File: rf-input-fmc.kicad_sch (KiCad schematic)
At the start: 0 parts

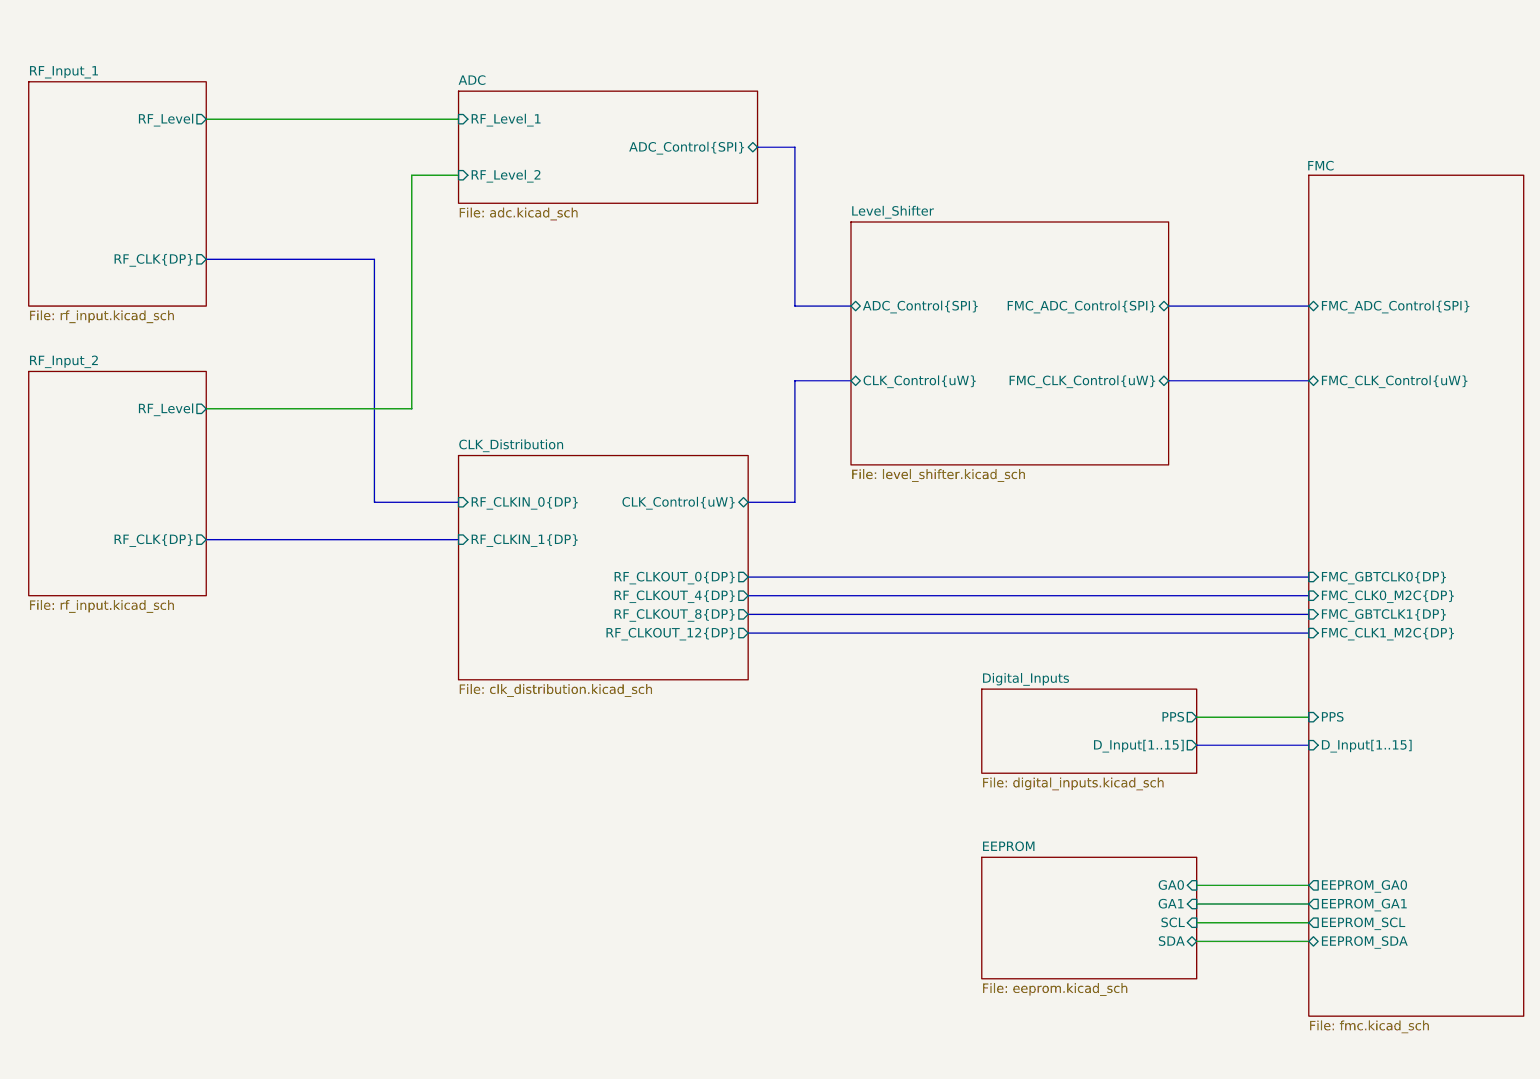
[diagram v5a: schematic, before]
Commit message: Changed ADC and removed Level Shifter
- Changed ADC to ADS7253
- Removed Level Shifters
- Change paper size to US standard sizes for printing
- removed 3d models
- Changed SMA clock input to a 2 pin ISORATE connector
- Floor planned out the PCB layout with the new parts
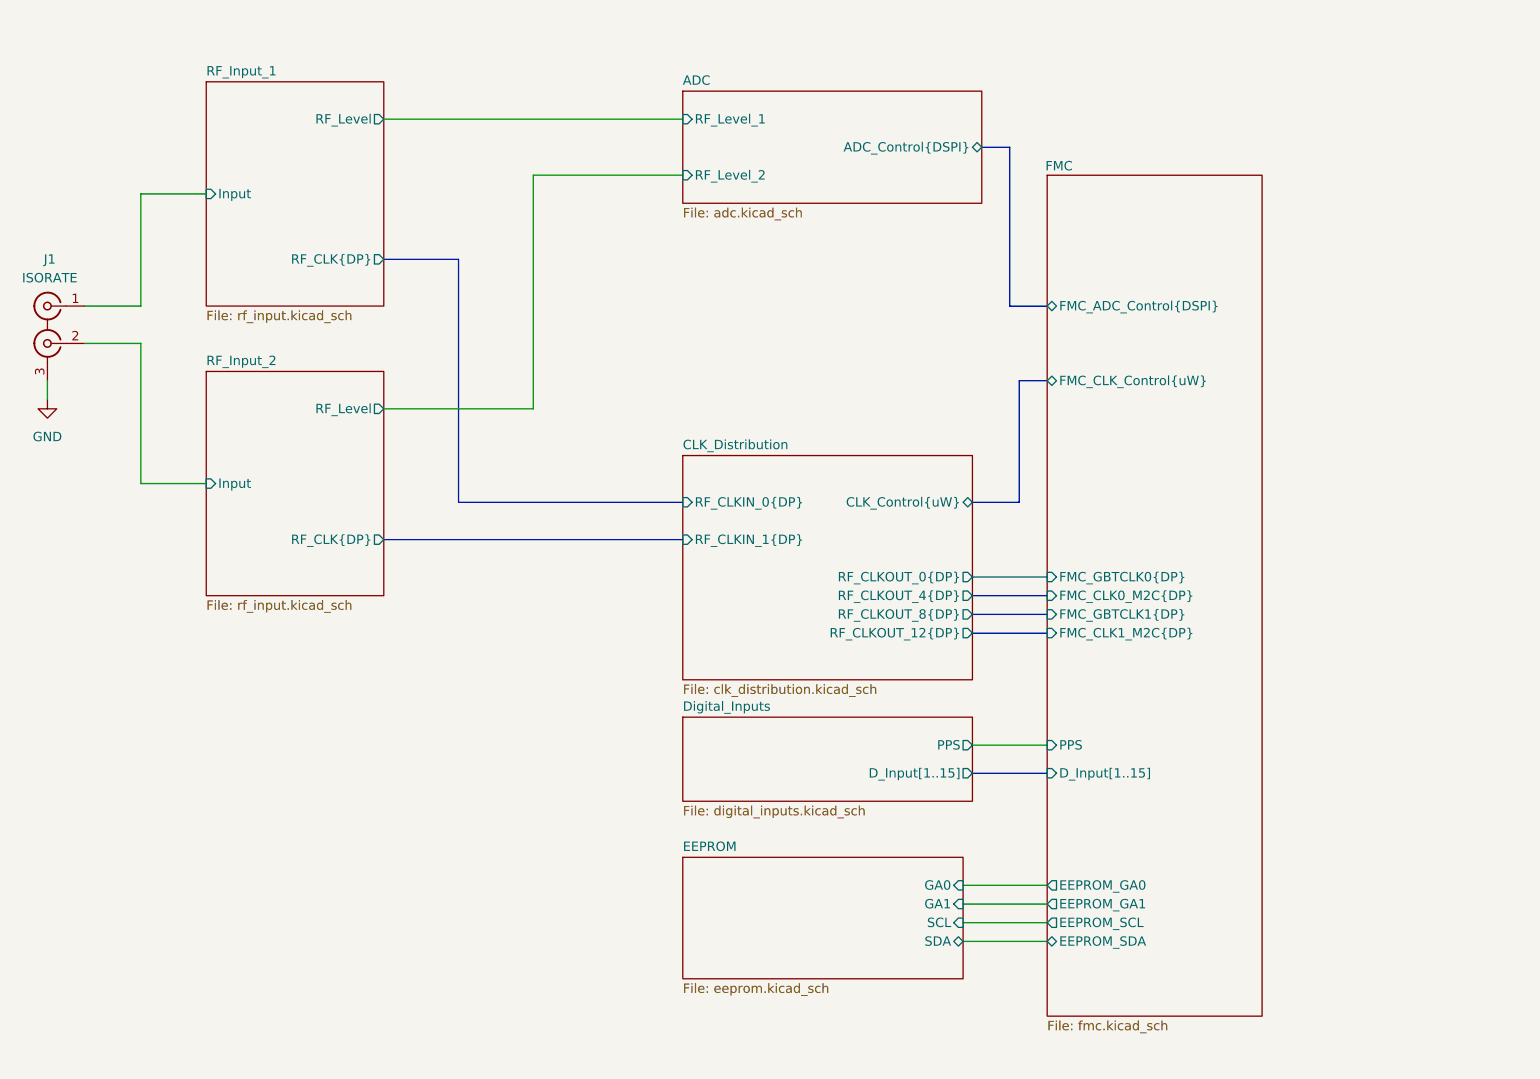
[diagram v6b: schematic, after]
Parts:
- added J1: ISORATE, rf-input-fmc:SAMTEC_IP5-02-01-L-S-RA1-L-TR, symbol Connector:Conn_Coaxial_x2
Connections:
- new net GND: J1.3 (EXT)
- new net RF_Input_1/Input: J1.1 (IN1)
- new net RF_Input_2/Input: J1.2 (IN2)
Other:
- removed sheet Level_Shifter
- sheet ADC ports: added ADC_Control{DSPI}; removed ADC_Control{SPI}
- sheet FMC ports: added FMC_ADC_Control{DSPI}; removed FMC_ADC_Control{SPI}
- sheet RF_Input_1 ports: added Input; removed none
- sheet RF_Input_2 ports: added Input; removed none

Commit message: Final Schmatic Draft
-Changed ADC
-Changed Digital IO Translator
-Updated all MPNs
- Reannoted Schematic
- Updated Design Document
- Added new Datasheet Document
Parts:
- J1: MPN (none) -> SAMTEC_IP5-02-01-L-S-RA1-L-TR; Manufacturer (none) -> Samtec
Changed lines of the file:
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@@
 			)
 		)
-		(property "Datasheet" ""
+		(property "Datasheet" "~"
 			(at 40.64 66.04 0)
 			(effects
@@
 			(at 40.64 63.5 0)
 			(effects
+				(font
+					(size 1.27 1.27)
+				)
+				(hide yes)
+			)
+		)
+		(property "MPN" "SAMTEC_IP5-02-01-L-S-RA1-L-TR"
+			(at 40.64 63.5 0)
+			(effects
+				(font
+					(size 1.27 1.27)
+				)
+				(hide yes)
+			)
+		)
+		(property "Manufacturer" "Samtec"
+			(at 40.64 63.5 0)
+			(effects

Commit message: Schematic updates
- Changed Connecters to MMCX
- Added Test points on clocks and data buses
- Added attenuation before the RF input level detection IC to better keep the recommended input within its linear range
- Added a low pass filter at the input of the RF input level detection IC
- grounded the thermal pad of the ADC
- added some additional decoupling caps in for the clock splitter chip (to be in line with what is on Zest)
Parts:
- removed J1: ISORATE, rf-input-fmc:SAMTEC_IP5-02-01-L-S-RA1-L-TR, symbol Connector:Conn_Coaxial_x2
- added J1, J2: MMCX, Connector_Coaxial:MMCX_Molex_73415-1471_Vertical, symbol Connector:Conn_Coaxial
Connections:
- net GND: now also J1.2 (Ext), J2.2 (Ext)
- net RF_Input_1/Input: now also J1.1 (In)
- net RF_Input_2/Input: now also J2.1 (In)
